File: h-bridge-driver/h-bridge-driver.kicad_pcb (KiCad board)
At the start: 4 copper layers, 31.8 x 35.6 mm, 38 parts, among them J1 CON_HDR_100MILS_M_TH_2X8, J2 CON_HDR_100MILS_M_TH_1X3, J3 CON_TERM_BLK_1X2_TB008A-508-0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, Q1 TRX_2NPN_BC846S,115, Q2 TRX_NMOS_PJD40N04_L2_00001, Q3 TRX_NMOS_PJD40N04_L2_00001, Q4 TRX_NMOS_PJD40N04_L2_00001, Q5 TRX_NMOS_PJD40N04_L2_00001, U1 DRV_A4957SESTR-T

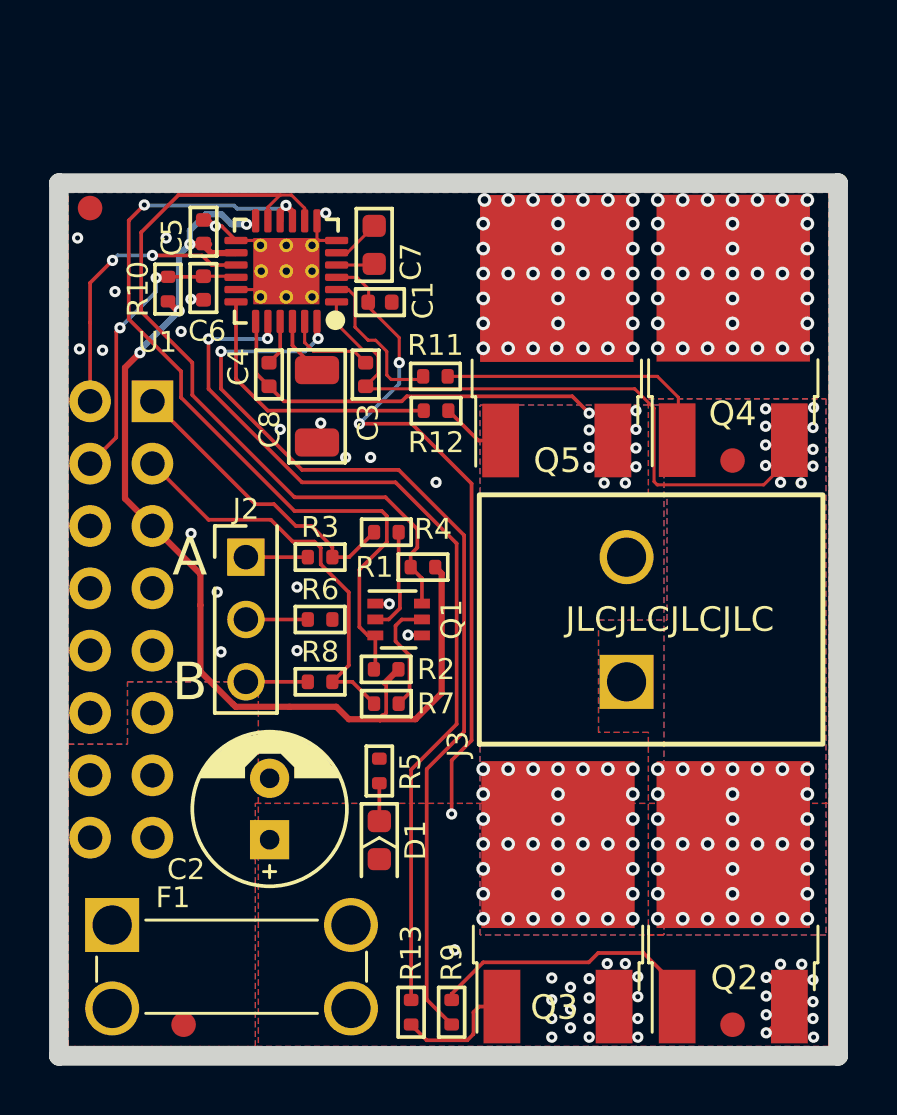
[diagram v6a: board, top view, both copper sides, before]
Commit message: Add Enclosure piercing guide and fix h-bridge-driver NMOS pads.
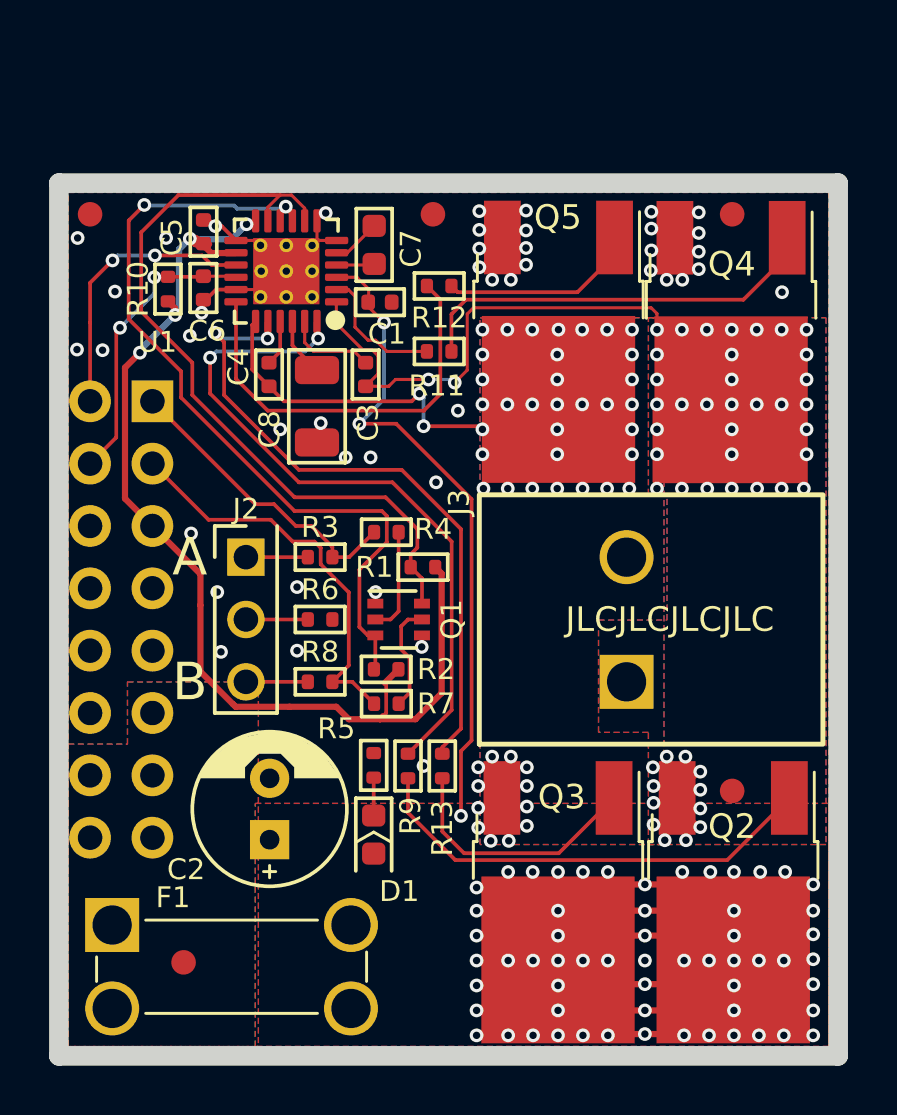
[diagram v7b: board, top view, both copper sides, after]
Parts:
- added F4: FID_1X1, connaxio-mechanical:FID_1X1, F.Cu at (129.2, 54.6)
- moved R9 10.2 mm to (128.1, 77.1), turned to -90 degrees
- moved R13 10.1 mm to (129.5, 77.1)
- moved F2 10.0 mm to (141.4, 54.6)
- moved F6 9.53 mm to (141.4, 78.1)
- moved R12 5.08 mm to (129.4, 57.5)
- moved F5 2.54 mm to (119.0, 85.1)
- moved R11 1.03 mm to (129.4, 60.2)
- moved D1 0.32 mm to (126.7, 79.9)
- moved R5 0.32 mm to (126.7, 77.1)
- moved Q4 0.27 mm to (141.3, 59.8), turned to 180 degrees
- moved F3 0.25 mm to (115.2, 54.6)
- moved Q5 0.24 mm to (134.3, 59.8), turned to 180 degrees
- turned Q2 to 180 degrees
- turned Q3 to 180 degrees
- renumbered F4 to F5, F5 to F6
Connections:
- F2 pad 1: /OUTA -> GND
- F6 pad 1: Vdrive -> /OUTA
- Q2 pad 2: Vdrive -> /OUTA
- Q2 pad 3: /OUTA -> Vdrive
- Q3 pad 2: Vdrive -> /OUTB
- Q3 pad 3: /OUTB -> Vdrive
- Q4 pad 2: /OUTA -> GND
- Q4 pad 3: GND -> /OUTA
- Q5 pad 2: /OUTB -> GND
- Q5 pad 3: GND -> /OUTB
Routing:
- net Vdrive: track 34.0 -> 80.3 mm, vias 31 -> 62
- net Net-(R9-Pad1): track 39.8 -> 28.6 mm
- net Net-(R13-Pad1): track 37.2 -> 27.0 mm
- net Net-(Q2-Pad1): track 11.5 -> 18.8 mm
- net /OUTA: track 26.3 -> 32.3 mm, vias 43 -> 47
- net Net-(R12-Pad1): track 11.3 -> 16.9 mm
- net Net-(Q5-Pad1): track 2.64 -> 8.10 mm
- net Net-(Q4-Pad1): track 11.5 -> 16.9 mm
- net Net-(Q3-Pad1): track 5.06 -> 10.5 mm
- net /OUTB: track 16.5 -> 13.3 mm, vias 43 -> 47
- net GND: track 12.5 -> 13.8 mm, vias 87 -> 44
- net Net-(R11-Pad1): track 6.40 -> 5.46 mm
- removed copper zone on In1.Cu, net /OUTA
- removed copper zone on In2.Cu, net /OUTA
- removed copper zone on In1.Cu, net /OUTB
- removed copper zone on In2.Cu, net /OUTB
- removed copper zone on In1.Cu, net /VIN
- removed copper zone on In2.Cu, net /VIN
- removed copper zone on In1.Cu, net GND
- removed copper zone on In2.Cu, net GND
- removed copper zone on In1.Cu, net Vdrive
- removed copper zone on In2.Cu, net Vdrive
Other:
- copper layers 4 -> 2

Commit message: Invert connectors (male/female) Replace TH connectors with SMD ones on mainboard Add 555 timer on simple-switch to generate 60 Hz Add jumper on simple-switch to select AC Add series I2C resistors on mainboard from mikroBUS socket
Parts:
- J1: value CON_HDR_100MILS_M_TH_2X8 -> CON_HDR_100MILS_F_TH_2X8; footprint connaxio-connectors:CON_HDR_100MILS_M_TH_2X8 -> connaxio-connectors:CON_HDR_100MILS_F_TH_2X8
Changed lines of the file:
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@@
       ) (layer "B.SilkS") (width 0) (fill solid))
   )
-  (footprint "connaxio-connectors:CON_HDR_100MILS_M_TH_2X8" (layer "B.Cu")
+  (footprint "connaxio-connectors:CON_HDR_100MILS_F_TH_2X8" (layer "B.Cu")
     (at 116.459 71.12 180)
     (descr "Through hole straight pin header, 2x8, 2.54mm pitch, double rows")
     (tags "Through hole pin header THT 2x12 2.54mm double row")
     (property "Current" "3A")
-    (property "Note" "Male")
+    (property "Note" "Female")
     (property "Package" "TH")
     (property "Polarized" "No")
@@
     (property "Voltage" "350V")
     (attr through_hole)
-    (fp_text reference "J1" (at -1.905 -10.922) (layer "B.SilkS")
+    (fp_text reference "J1" (at -2.032 -11.049) (layer "B.SilkS")
       (effects (font (size 0.85 0.85) (thickness 0.15)) (justify mirror))
     )
-    (fp_text value "CON_HDR_100MILS_M_TH_2X8" (at 0 -16.3) (layer "B.Fab")
+    (fp_text value "CON_HDR_100MILS_F_TH_2X8" (at 0 -16.3) (layer "B.Fab")
       (effects (font (size 1 1) (thickness 0.15)) (justify mirror))
     )
@@
     )
     (fp_line (start 0 10.16) (end 2.54 10.16) (layer "B.SilkS") (width 0.15))
+    (fp_line (start -2.54 -10.16) (end 2.54 -10.16) (layer "B.SilkS") (width 0.15))
+    (fp_line (start -2.54 7.62) (end -2.54 -10.16) (layer "B.SilkS") (width 0.15))
+    (fp_line (start -2.54 10.16) (end -1.27 10.16) (layer "B.SilkS") (width 0.15))
     (fp_line (start 2.54 10.16) (end 2.54 -10.16) (layer "B.SilkS") (width 0.15))
-    (fp_line (start -2.54 10.16) (end -1.27 10.16) (layer "B.SilkS") (width 0.15))
     (fp_line (start -2.54 8.89) (end -2.54 10.16) (layer "B.SilkS") (width 0.15))
-    (fp_line (start -2.54 7.62) (end -2.54 -10.16) (layer "B.SilkS") (width 0.15))
-    (fp_line (start -2.54 -10.16) (end 2.54 -10.16) (layer "B.SilkS") (width 0.15))
+    (fp_line (start -3.048 10.668) (end -3.048 -10.668) (layer "B.CrtYd") (width 0.05))
     (fp_line (start 3.048 -10.668) (end 3.048 10.668) (layer "B.CrtYd") (width 0.05))
     (fp_line (start 3.048 10.668) (end -3.048 10.668) (layer "B.CrtYd") (width 0.05))
     (fp_line (start -3.048 -10.668) (end 3.048 -10.668) (layer "B.CrtYd") (width 0.05))
-    (fp_line (start -3.048 10.668) (end -3.048 -10.668) (layer "B.CrtYd") (width 0.05))
     (fp_line (start -2.54 -10.16) (end -2.54 10.16) (layer "B.Fab") (width 0.1))
+    (fp_line (start -2.54 8.89) (end -1.27 10.16) (layer "B.Fab") (width 0.1))
     (fp_line (start 2.54 10.16) (end 2.54 -10.16) (layer "B.Fab") (width 0.1))
     (fp_line (start 2.54 -10.16) (end -2.54 -10.16) (layer "B.Fab") (width 0.1))
-    (fp_line (start -2.54 8.89) (end -1.27 10.16) (layer "B.Fab") (width 0.1))
     (fp_line (start -1.27 10.16) (end 2.54 10.16) (layer "B.Fab") (width 0.1))
     (pad "1" thru_hole rect (at -1.27 8.89 180) (size 1.7 1.7) (drill 1) (layers *.Cu *.Mask)
@@
     (pad "16" thru_hole oval (at 1.27 -8.89 180) (size 1.7 1.7) (drill 1) (layers *.Cu *.Mask)
       (net 24 "/VIN") (pinfunction "16") (pintype "passive"))
-    (model ":CONNAXIO_KICAD_LIB_DIR:connaxio-connectors.3dshapes/CON_HDR_100MILS_M_TH_2X8.wrl"
-      (offset (xyz -1.27 8.89 0))
+    (model ":CONNAXIO_KICAD_LIB_DIR:connaxio-connectors.3dshapes/CON_HDR_100MILS_F_TH_2X8.wrl"
+      (offset (xyz 1.27 8.89 0))
       (scale (xyz 1 1 1))
       (rotate (xyz 0 0 0))
